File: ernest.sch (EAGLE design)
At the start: 29 parts, among them IC1 ATMEGA328-P, SW1 IDENT, Y1 16MHz

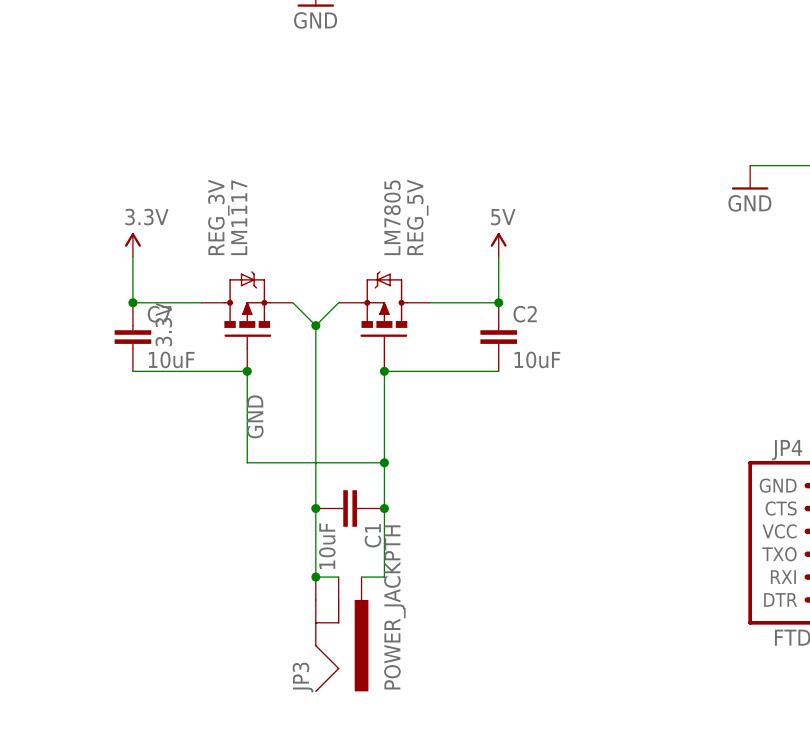
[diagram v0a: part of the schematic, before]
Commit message: Remove unnecessary 5v reg
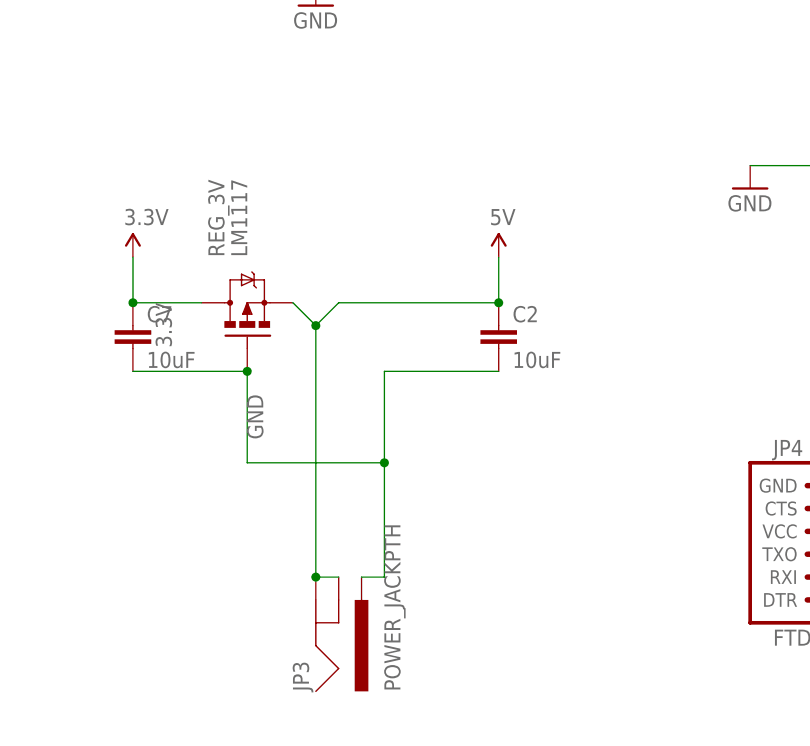
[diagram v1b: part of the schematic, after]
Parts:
- removed C1: 10uF, SparkFun-Capacitors:CAPPTH
- removed REG_5V: LM7805, User-Submitted:MOSFET-PCHANNELFQP27P06
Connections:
- removed net N$18: C1.2, JP3.GND, JP3.GNDBREAK, REG_3V.S, REG_5V.S
- net 5V: now also JP3.GND, JP3.GNDBREAK, REG_3V.S; no longer REG_5V.D
- net GND: no longer C1.1, REG_5V.G
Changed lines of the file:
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@@
 <part name="IC1" library="Arduino-AVR" deviceset="ATMEGA168-PU" device="" value="ATMEGA328-P"/>
 <part name="U$1" library="GeekAmmo" deviceset="TACTILE-SWITCH" device="-PTH"/>
-<part name="C1" library="SparkFun-Capacitors" deviceset="CAP" device="PTH" value="10uF"/>
 <part name="C2" library="SparkFun-Capacitors" deviceset="CAP" device="PTH" value="10uF"/>
 <part name="Y1" library="SparkFun-FreqCtrl" deviceset="CRYSTAL" device="HC49US" value="16MHz"/>
@@
 <part name="C5" library="SparkFun-Capacitors" deviceset="CAP" device="PTH" value="0.1uF"/>
 <part name="JP3" library="SparkFun-Connectors" deviceset="POWER_JACK" device="PTH"/>
-<part name="REG_5V" library="User-Submitted" deviceset="MOSFET-PCHANNEL" device="FQP27P06" value="LM7805"/>
 <part name="REG_3V" library="User-Submitted" deviceset="MOSFET-PCHANNEL" device="FQP27P06" value="LM1117"/>
 <part name="BMP180" library="SparkFun-Connectors" deviceset="M05" device="PTH" value="BMP"/>
@@
 <instance part="IC1" gate="1" x="-83.82" y="50.8"/>
 <instance part="U$1" gate="G$1" x="-134.62" y="81.28"/>
-<instance part="C1" gate="G$1" x="-111.76" y="-43.18" rot="R270"/>
 <instance part="C2" gate="G$1" x="-93.98" y="-25.4"/>
 <instance part="Y1" gate="G$1" x="-121.92" y="60.96" rot="R90"/>
@@
 <instance part="C5" gate="G$1" x="33.02" y="2.54"/>
 <instance part="JP3" gate="G$1" x="-116.84" y="-53.34" rot="MR90"/>
-<instance part="REG_5V" gate="G$1" x="-106.68" y="-20.32" rot="MR90"/>
 <instance part="REG_3V" gate="G$1" x="-121.92" y="-20.32" rot="R90"/>
 <instance part="BMP180" gate="G$1" x="-7.62" y="2.54"/>
@@
 <wire x1="-121.92" y1="-38.1" x2="-121.92" y2="-27.94" width="0.1524" layer="91"/>
 <label x="-121.92" y="-30.48" size="1.778" layer="95" rot="R270"/>
-<pinref part="REG_5V" gate="G$1" pin="G"/>
 <wire x1="-106.68" y1="-27.94" x2="-93.98" y2="-27.94" width="0.1524" layer="91"/>
 <pinref part="C2" gate="G$1" pin="2"/>
 <pinref part="JP3" gate="G$1" pin="PWR"/>
-<pinref part="C1" gate="G$1" pin="1"/>
 <wire x1="-109.22" y1="-50.8" x2="-106.68" y2="-50.8" width="0.1524" layer="91"/>
-<wire x1="-106.68" y1="-50.8" x2="-106.68" y2="-43.18" width="0.1524" layer="91"/>
+<wire x1="-106.68" y1="-50.8" x2="-106.68" y2="-38.1" width="0.1524" layer="91"/>
 <wire x1="-106.68" y1="-27.94" x2="-106.68" y2="-38.1" width="0.1524" layer="91"/>
-<junction x="-106.68" y="-27.94"/>
-<junction x="-106.68" y="-43.18"/>
-<wire x1="-106.68" y1="-38.1" x2="-106.68" y2="-43.18" width="0.1524" layer="91"/>
 <wire x1="-121.92" y1="-38.1" x2="-106.68" y2="-38.1" width="0.1524" layer="91"/>
 <junction x="-106.68" y="-38.1"/>
@@
 <wire x1="-53.34" y1="25.4" x2="-45.72" y2="25.4" width="0.1524" layer="91"/>
 <label x="-50.8" y="25.4" size="1.778" layer="95"/>
-</segment>
-</net>
-<net name="N$18" class="0">
-<segment>
-<pinref part="C1" gate="G$1" pin="2"/>
-<pinref part="JP3" gate="G$1" pin="GND"/>
-<wire x1="-114.3" y1="-43.18" x2="-114.3" y2="-50.8" width="0.1524" layer="91"/>
-<pinref part="JP3" gate="G$1" pin="GNDBREAK"/>
-<wire x1="-111.76" y1="-50.8" x2="-114.3" y2="-50.8" width="0.1524" layer="91"/>
-<junction x="-114.3" y="-50.8"/>
-<pinref part="REG_5V" gate="G$1" pin="S"/>
-<wire x1="-111.76" y1="-20.32" x2="-114.3" y2="-22.86" width="0.1524" layer="91"/>
-<wire x1="-114.3" y1="-22.86" x2="-114.3" y2="-43.18" width="0.1524" layer="91"/>
-<junction x="-114.3" y="-43.18"/>
-<pinref part="REG_3V" gate="G$1" pin="S"/>
-<wire x1="-114.3" y1="-22.86" x2="-116.84" y2="-20.32" width="0.1524" layer="91"/>
-<junction x="-114.3" y="-22.86"/>
 </segment>
 </net>
@@
 <segment>
 <pinref part="C2" gate="G$1" pin="1"/>
-<pinref part="REG_5V" gate="G$1" pin="D"/>
-<wire x1="-101.6" y1="-20.32" x2="-93.98" y2="-20.32" width="0.1524" layer="91"/>
 <pinref part="SUPPLY3" gate="G$1" pin="5V"/>
 <wire x1="-93.98" y1="-20.32" x2="-93.98" y2="-15.24" width="0.1524" layer="91"/>
 <junction x="-93.98" y="-20.32"/>
-</segment>
-<segment>
+<pinref part="JP3" gate="G$1" pin="GND"/>
+<pinref part="JP3" gate="G$1" pin="GNDBREAK"/>
+<wire x1="-111.76" y1="-50.8" x2="-114.3" y2="-50.8" width="0.1524" layer="91"/>
+<junction x="-114.3" y="-50.8"/>
+<wire x1="-111.76" y1="-20.32" x2="-114.3" y2="-22.86" width="0.1524" layer="91"/>
+<wire x1="-114.3" y1="-22.86" x2="-114.3" y2="-50.8" width="0.1524" layer="91"/>
+<pinref part="REG_3V" gate="G$1" pin="S"/>
+<wire x1="-114.3" y1="-22.86" x2="-116.84" y2="-20.32" width="0.1524" layer="91"/>
+<junction x="-114.3" y="-22.86"/>
+<wire x1="-111.76" y1="-20.32" x2="-93.98" y2="-20.32" width="0.1524" layer="91"/>
+</segment>
+<segment>

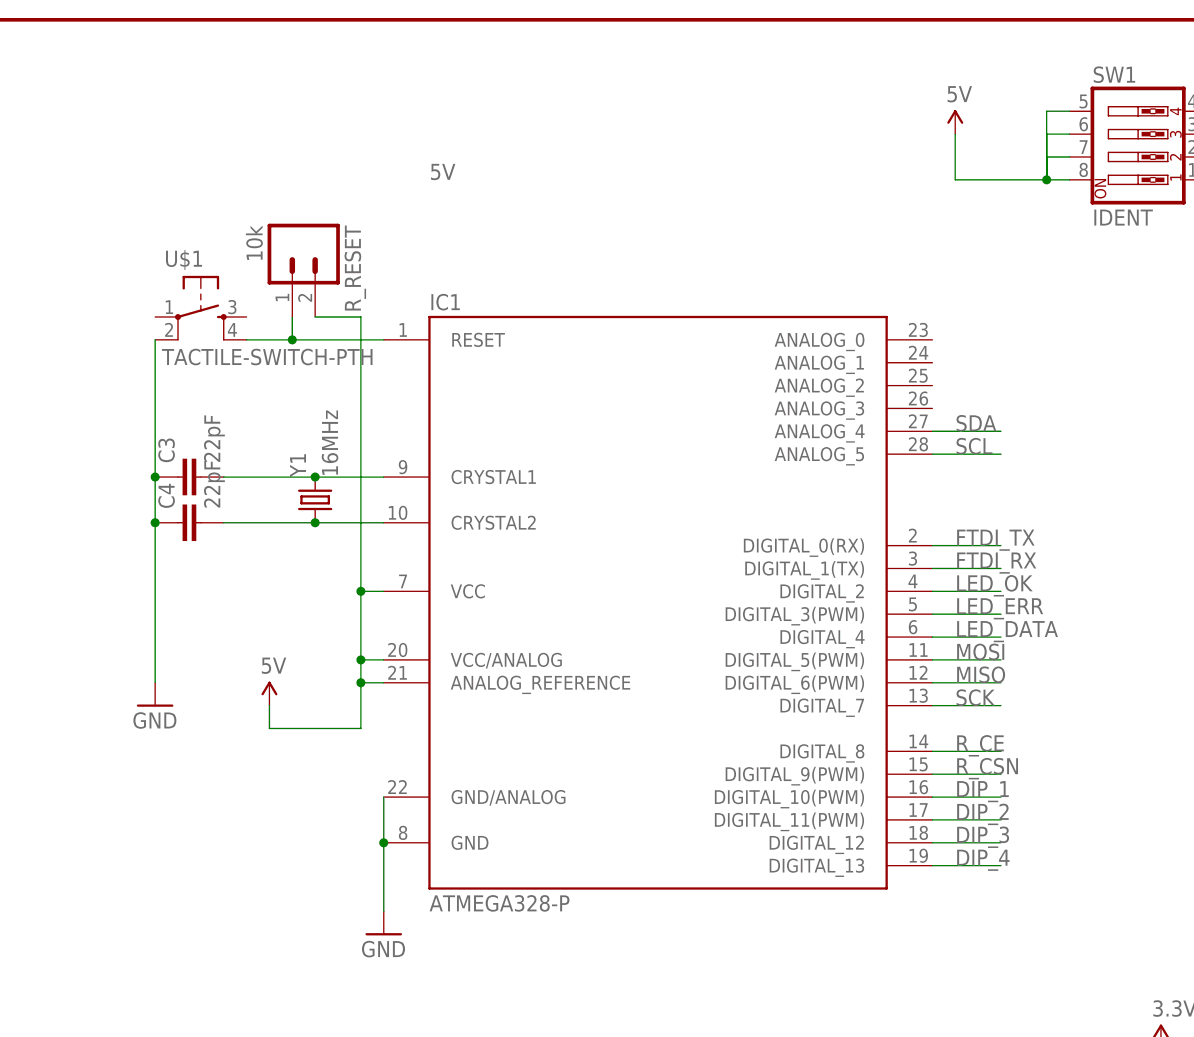
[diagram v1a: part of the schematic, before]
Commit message: Reorder SPI pins based off breadboard test
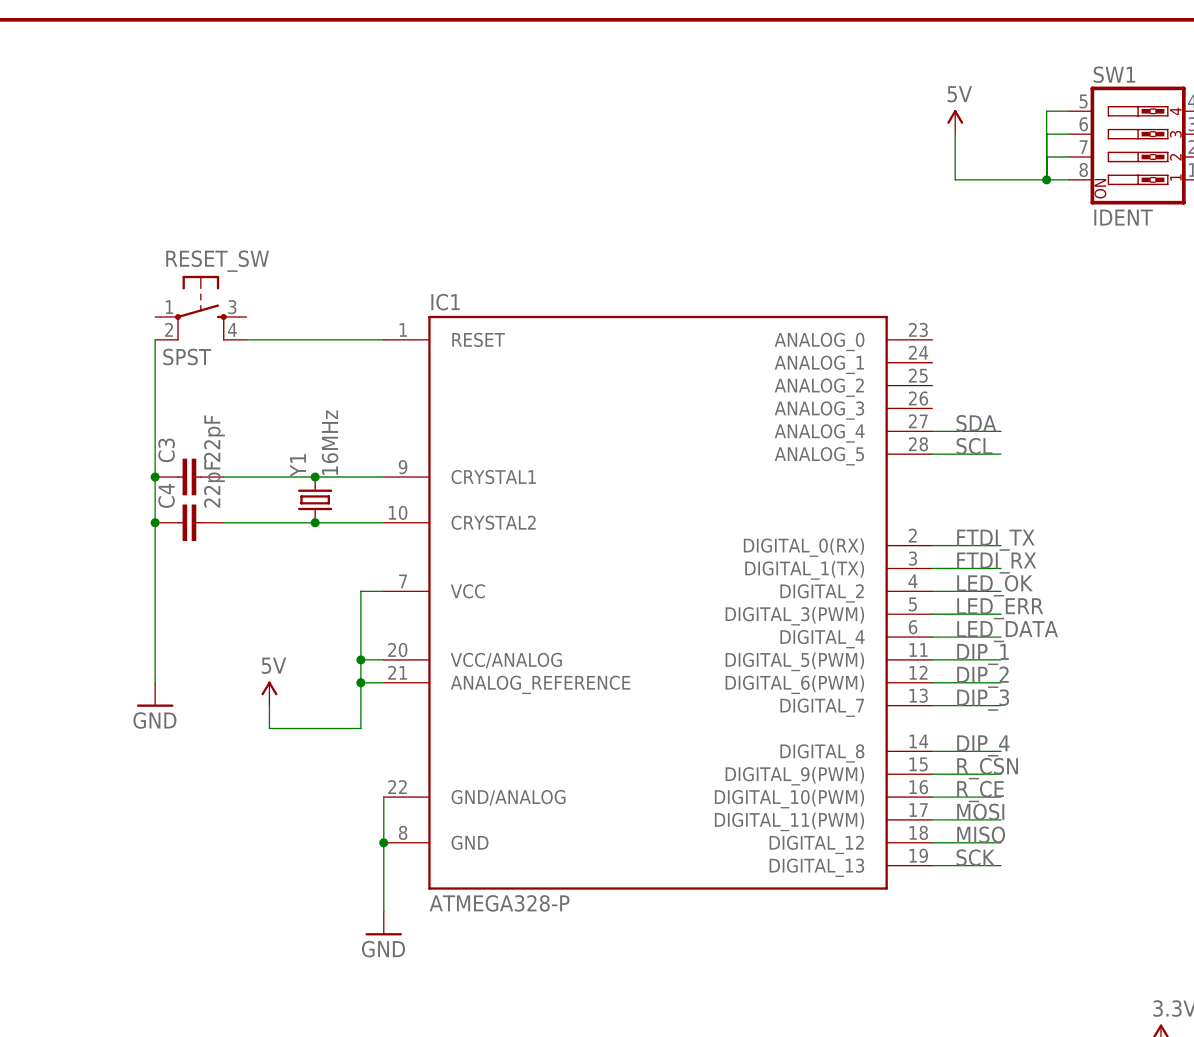
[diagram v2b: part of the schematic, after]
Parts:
- removed R_RESET: 10k, SparkFun-Connectors:M02PTH
- RESET_SW: value TACTILE-SWITCH-PTH -> SPST
- renumbered U$1 to RESET_SW
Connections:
- net 5V: no longer R_RESET.2
- net DIP_1: now also IC1.DIGITAL_5(PWM); no longer IC1.DIGITAL_10(PWM)
- net DIP_2: now also IC1.DIGITAL_6(PWM); no longer IC1.DIGITAL_11(PWM)
- net DIP_3: now also IC1.DIGITAL_7; no longer IC1.DIGITAL_12
- net DIP_4: now also IC1.DIGITAL_8; no longer IC1.DIGITAL_13
- net MISO: now also IC1.DIGITAL_12; no longer IC1.DIGITAL_6(PWM)
- net MOSI: now also IC1.DIGITAL_11(PWM); no longer IC1.DIGITAL_5(PWM)
- net N$12: no longer R_RESET.1
- net R_CE: now also IC1.DIGITAL_10(PWM); no longer IC1.DIGITAL_8
- net SCK: now also IC1.DIGITAL_13; no longer IC1.DIGITAL_7

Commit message: V0.4 release
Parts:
- removed ERNEST: Ernest, SparkFun-Aesthetics:FRAME-LETTER
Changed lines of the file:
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@@
 <part name="REG_3V" library="User-Submitted" deviceset="MOSFET-PCHANNEL" device="FQP27P06" value="LM1117"/>
 <part name="BMP180" library="SparkFun-Connectors" deviceset="M05" device="PTH" value="BMP"/>
-<part name="ERNEST" library="SparkFun-Aesthetics" deviceset="FRAME-LETTER" device="" value="Ernest">
-<attribute name="DESIGNER" value="Ross Schlaikjer"/>
-<attribute name="VERSION" value="v0.4"/>
-</part>
 <part name="JP4" library="SparkFun-Connectors" deviceset="ARDUINO_SERIAL_PROGRAM" device="PTH" value="FTDI"/>
 <part name="SUPPLY1" library="SparkFun-Aesthetics" deviceset="3.3V" device=""/>
@@
 <instance part="REG_3V" gate="G$1" x="-121.92" y="-20.32" rot="R90"/>
 <instance part="BMP180" gate="G$1" x="-7.62" y="2.54"/>
-<instance part="ERNEST" gate="G$1" x="-160.02" y="-71.12"/>
-<instance part="ERNEST" gate="V" x="-12.7" y="-71.12"/>
 <instance part="JP4" gate="G$1" x="-58.42" y="-48.26"/>
 <instance part="SUPPLY1" gate="G$1" x="7.62" y="12.7"/>
